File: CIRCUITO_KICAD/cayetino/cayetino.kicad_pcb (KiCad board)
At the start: 2 copper layers, 2 parts

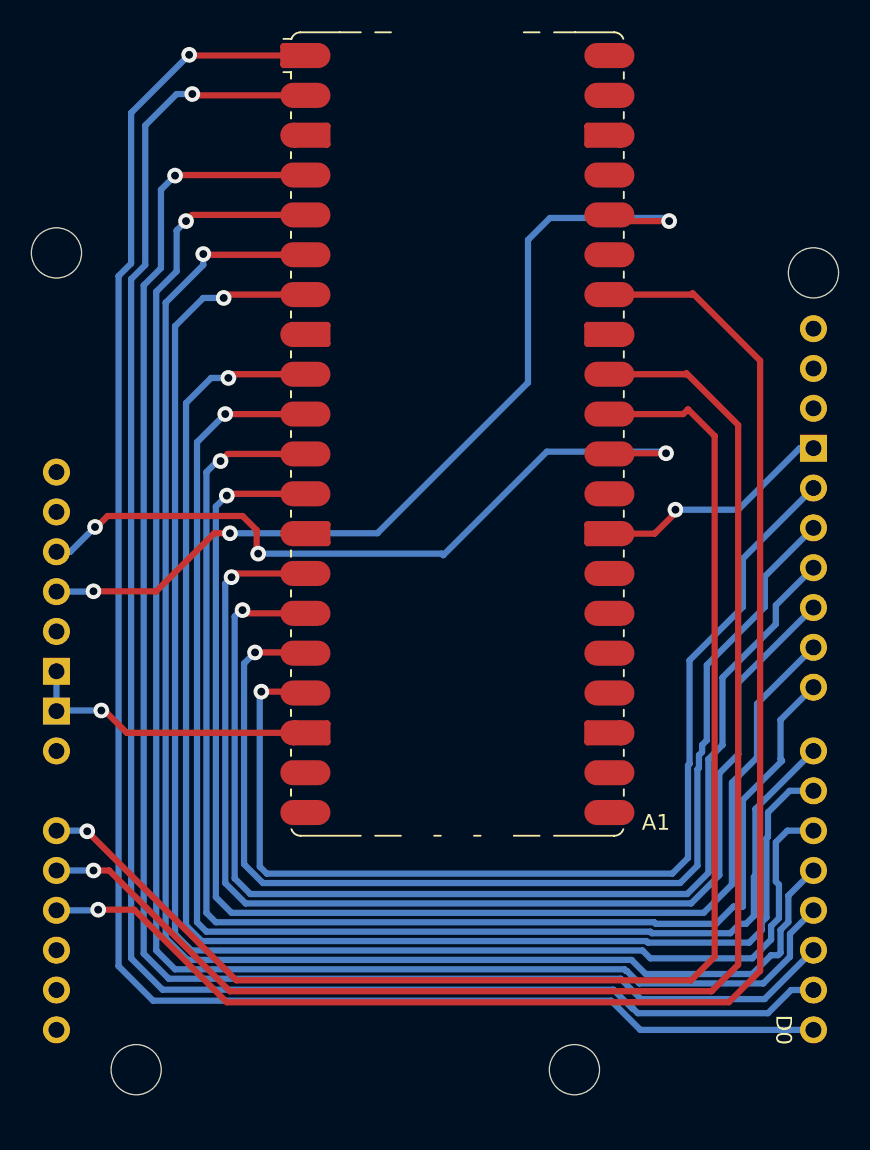
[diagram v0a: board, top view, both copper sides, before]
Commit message: Add Micro SD Card Socket with detection pin to Cayetino project
- Updated `cayetino.kicad_pro` to include new designator for the Micro SD Card Socket (J1).
- Added Micro SD Card Socket symbol and properties in `cayetino.kicad_sch`.
- Included necessary pin configurations and labels for the Micro SD Card Socket.
- Created a new `report.txt` file for project documentation.
- Added a lock file `~cayetino.kicad_pro.lck` for project management.
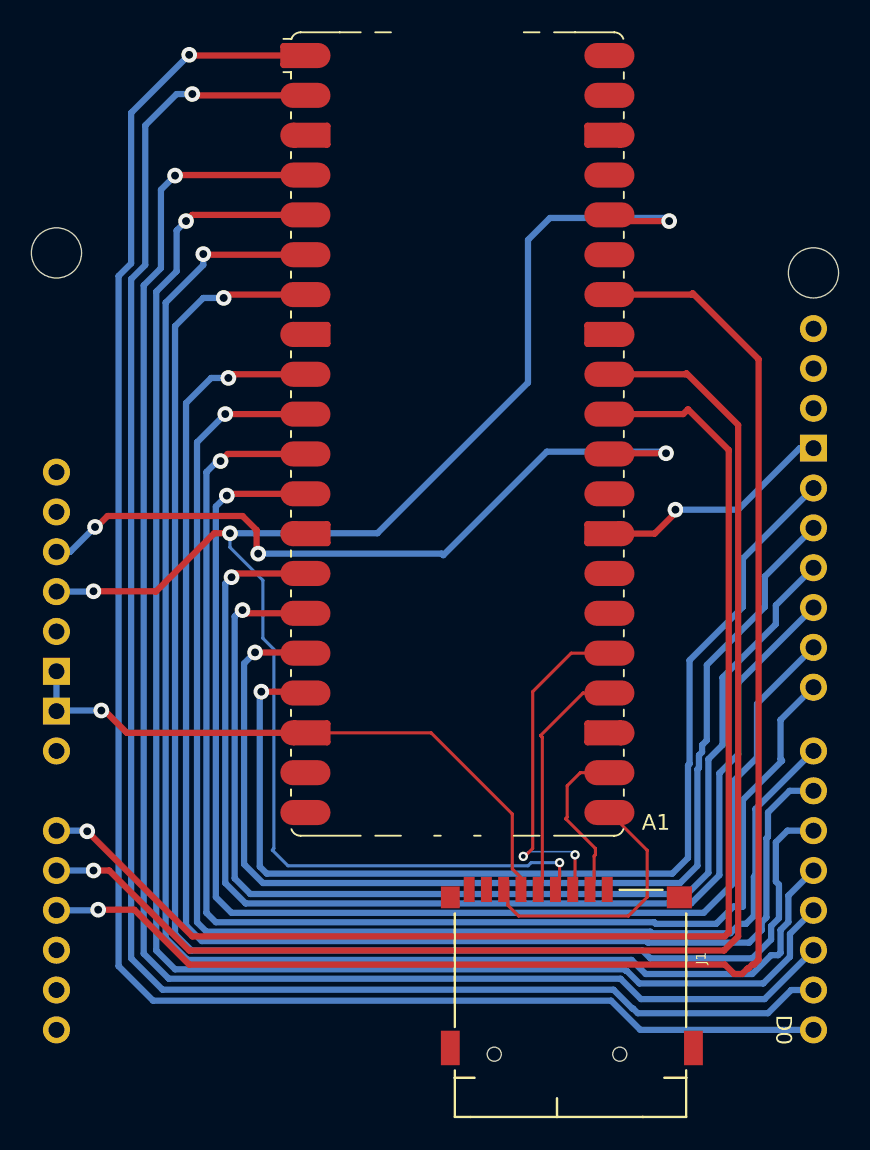
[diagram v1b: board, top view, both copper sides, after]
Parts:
- added J1: Micro_SD_Card_Det1, Module:J_SD_Card-micro_socket_A, F.Cu at (126.1, 101.3)
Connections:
- net Net-(A1-3V3) renamed /3V3
- A1 pad 13: Net-(A1-GND-Pad13) -> /GND
- A1 pad 18: Net-(A1-GND-Pad13) -> /GND
- A1 pad 21: unconnected-(A1-GPIO16-Pad21) -> /MISO
- A1 pad 22: unconnected-(A1-GPIO17-Pad22) -> /CS
- A1 pad 23: Net-(A1-GND-Pad13) -> /GND
- A1 pad 24: unconnected-(A1-GPIO18-Pad24) -> /SCK
- A1 pad 25: unconnected-(A1-GPIO19-Pad25) -> /MOSI
- A1 pad 28: Net-(A1-GND-Pad13) -> /GND
- A1 pad 3: Net-(A1-GND-Pad13) -> /GND
- A1 pad 33: unconnected-(A1-AGND-Pad33) -> /GND
- A1 pad 38: Net-(A1-GND-Pad13) -> /GND
- A1 pad 8: Net-(A1-GND-Pad13) -> /GND
- A2 pad GND1: Net-(A1-GND-Pad13) -> /GND
- A2 pad GND2: Net-(A1-GND-Pad13) -> /GND
- A2 pad GND3: Net-(A1-GND-Pad13) -> /GND
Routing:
- net /GND: track 0.00 -> 54.9 mm, vias 0 -> 2
- net /3V3: track 58.3 -> 99.8 mm, vias 3 -> 4
- net Net-(A1-GND-Pad13): track 34.5 -> 0.00 mm, vias 2 -> 0
- net /MOSI: track 0.00 -> 21.9 mm, vias 0 -> 2
- net /MISO: track 0.00 -> 17.6 mm
- net /SCK: track 0.00 -> 14.8 mm
- net /CS: track 0.00 -> 9.98 mm
- net Net-(A1-GPIO27_ADC1): track 91.5 -> 88.2 mm
- net Net-(A1-GPIO28_ADC2): track 98.5 -> 96.4 mm
- net Net-(A1-GPIO26_ADC0): track 87.3 -> 85.3 mm
